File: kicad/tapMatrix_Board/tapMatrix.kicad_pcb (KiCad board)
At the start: 2 copper layers, 68.6 x 53.3 mm, 31 parts, among them P5 TS_ZIF, P6 LED_MATRIX_HDR, U1 MCP1703, U2 MCP4921-E/SN, U3 74LS125, U4 TS922, U5 SD_CARD, U6 DS3231

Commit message: Rough placement of footprints
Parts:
- removed JP7: 6_PIN_3, tapmatrix:Pin_Header_Straight_1x06
- added C10: 47uF, CAP_MVA_F55, F.Cu at (162.8, 128.3)
- added C11: 47uF, CAP_MVA_F55, F.Cu at (184.2, 128.4)
- added C12: 0.1uF, tapmatrix:C_0603, F.Cu at (183.9, 123.4)
- added C13: 0.1uF, tapmatrix:C_0603, F.Cu at (158.9, 109.1)
- added C14: 0.1uF, tapmatrix:C_0603, F.Cu at (143.5, 86.5)
- added C15: 47pF, tapmatrix:C_0603, F.Cu at (143.5, 88.9)
- added C16: 47pF, tapmatrix:C_0603, F.Cu at (143.5, 91.3)
- added C17: 4.7uF, EEE-0JA101WR, F.Cu at (134.6, 99.9)
- added C18: 0.1uF, tapmatrix:C_0603, F.Cu at (143.5, 93.3)
- added C19: 0.1uF, tapmatrix:C_0603, F.Cu at (143.5, 95.4)
- added D1: DIODE, DS16004, F.Cu at (153.7, 126.7)
- added D2: LED, D_0603, F.Cu at (190.6, 129.9)
- added D3: LED, D_0603, F.Cu at (153.0, 105.8)
- added D4: TXLED, D_0603, F.Cu at (146.1, 106.0)
- added D5: RXLED, D_0603, F.Cu at (143.9, 98.9)
- added F1: 500mA, Fuse_MF_MSMF, F.Cu at (156.1, 87.5)
- added P1: +9V Power, tapmatrix:PJ-102AH, F.Cu at (144.7, 132.2)
- added P2: USB-MINI-B, tapmatrix:USBMiniB_UX60_MB_5S8, F.Cu at (138.3, 90.2)
- added R10: 1K, tapmatrix:R_0603, F.Cu at (146.9, 98.9)
- added R11: 10K, tapmatrix:R_0603, F.Cu at (158.5, 102.0)
- added R12: 1K, tapmatrix:R_0603, F.Cu at (161.2, 102.0)
- added R13: 10K, tapmatrix:R_0603, F.Cu at (163.7, 102.0)
- added R14: 1K, tapmatrix:R_0603, F.Cu at (141.2, 98.9)
- added R15: 1K, R_0603, F.Cu at (141.2, 105.9)
- added R6: 510, tapmatrix:R_0603, F.Cu at (190.5, 125.3)
- added R7: 510, tapmatrix:R_0603, F.Cu at (150.2, 105.8)
- added R8: 27, tapmatrix:R_0603, F.Cu at (150.1, 89.2)
- added R9: 27, tapmatrix:R_0603, F.Cu at (150.1, 94.0)
- added SW1: SW_PUSH, SW_3BU_1000P, F.Cu at (162.8, 87.5)
- added U10: 2N7002PW, tapmatrix:SOT-323, F.Cu at (162.7, 97.3)
- added U7: NCP1117ST50T3G, SOT223_318H, F.Cu at (169.7, 128.4)
- added U8: ATMEGA328P-A, tapmatrix:TQFP-32_7x7mm_Pitch0.8mm, F.Cu at (166.1, 114.2)
- added U9: FT231XS, SSOP20_FTDI231X, F.Cu at (156.0, 95.1)
- added X1: CRYSTAL_SMD, XTAL_CSTCE_V, F.Cu at (173.6, 118.7)
- BT1: value CR2032 -> BATTERY
- C4, C6, C9: footprint tapmatrix:EEE-0JA101WR -> EEE-0JA101WR
- JP1: value 6_PIN_1 -> FTDI
- JP2: value 6_PIN_2 -> nRF8001; footprint tapmatrix:Pin_Header_Straight_1x06 -> tapmatrix:Pin_Header_Straight_1x10
- JP3: value 8_PIN_1 -> ICSP; footprint tapmatrix:Pin_Header_Straight_1x08 -> tapmatrix:Pin_Header_Straight_2x03
- JP4: value 8_PIN_2 -> 4_PIN_2
- U2: footprint SOIC-8_N -> tapmatrix:SOIC-8_N
- U3: value 74LS125 -> 74AHC125
- U4: footprint TS922_SO8 -> tapmatrix:TS922_SO8
- U5: footprint 114-00841-68 -> tapmatrix:114-00841-68; moved to B.Cu
- U6: moved to B.Cu
- moved P5 57.0 mm to (189.1, 96.0), turned to 90 degrees
- moved C4 46.0 mm to (134.7, 118.7), turned to 90 degrees
- moved JP6 42.7 mm to (184.9, 104.4), turned to 90 degrees
- moved C6 40.8 mm to (134.7, 109.1), turned to 90 degrees
- moved C9 38.0 mm to (177.4, 96.1)
- moved C2 38.0 mm to (143.3, 120.7)
- moved JP5 37.7 mm to (184.9, 95.6), turned to 270 degrees
- moved C3 34.5 mm to (143.3, 115.7)
- moved RV1 33.5 mm to (191.5, 104.3)
- moved R5 31.4 mm to (158.0, 121.7), turned to 90 degrees
- moved C1 29.6 mm to (143.1, 125.0), turned to 0 degrees
- moved U1 25.9 mm to (136.1, 125.2), turned to 270 degrees
- moved U3 22.4 mm to (152.1, 115.1), turned to 270 degrees
- moved C5 22.1 mm to (143.5, 110.4)
- moved U5 21.6 mm to (132.2, 107.8), turned to 90 degrees
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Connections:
- JP1 pad 1: Net-(JP1-Pad1) -> GND
- JP1 pad 2: Net-(JP1-Pad2) -> GND
- JP1 pad 4: GND -> /MATRIX_CS
- JP1 pad 5: GND -> /MATRIX_CLK
- JP1 pad 6: Net-(JP1-Pad6) -> /RESET
- JP2 pad 1: /XM -> /SCK
- JP2 pad 2: /YP -> /MISO
- JP2 pad 3: /XP -> /MOSI
- JP2 pad 4: /YM -> /D8
- JP2 pad 5: /I2C_SDA -> /DAC_SCK
- JP2 pad 6: /I2C_SCL -> Net-(JP2-Pad6)
- JP3 pad 1: Net-(JP3-Pad1) -> /MISO
- JP3 pad 2: GND -> +5V
- JP3 pad 4: /MISO -> /MOSI
- JP3 pad 5: /MOSI -> /RESET
- JP3 pad 6: /SD_CS -> GND
- JP4 pad 1: /MATRIX_DATA -> /I2C_SDA
- JP4 pad 2: /MATRIX_WR -> /I2C_SCL
- JP4 pad 3: /DAC_LAT -> +3.3V
- JP4 pad 4: /DAC_DI -> GND
- JP4 pad 5: /DAC_SCK -> (no net)
- JP4 pad 6: /DAC_CS -> (no net)
- JP4 pad 7: /MATRIX_CS -> (no net)
- JP4 pad 8: /MATRIX_CLK -> (no net)
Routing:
- net +3.3V: track 112.0 -> 0.00 mm, vias 2 -> 0
- net /I2C_SDA: track 96.3 -> 0.00 mm, vias 3 -> 0
- net /I2C_SCL: track 79.2 -> 0.00 mm, vias 6 -> 0
- net GND: track 76.8 -> 0.00 mm, vias 18 -> 0
- net /YM: track 56.1 -> 0.00 mm, vias 2 -> 0
- net Net-(BT1-Pad1): track 53.6 -> 0.00 mm, vias 2 -> 0
- net Net-(C9-Pad1): track 51.3 -> 0.00 mm, vias 4 -> 0
- net /XP: track 51.0 -> 0.00 mm, vias 2 -> 0
- net /YP: track 46.0 -> 0.00 mm, vias 2 -> 0
- net /XM: track 40.3 -> 0.00 mm, vias 2 -> 0
- net /SCLK: track 35.6 -> 0.00 mm, vias 2 -> 0
- net /DATA_IN: track 31.8 -> 0.00 mm, vias 2 -> 0
- net /CS: track 31.0 -> 0.00 mm
- net /MISO: track 30.6 -> 0.00 mm, vias 1 -> 0
- net /MATRIX_DATA: track 29.4 -> 0.00 mm
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- removed copper zone on F.Cu, net +5V
- removed copper zone on B.Cu, net GND
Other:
- board text removed: "(c) 2015 Responsive Devices Inc"
- board text removed: "3V3"
- board text removed: "5V0"
- board text removed: "922IY ST"
- board text removed: "SPK+"
- board text removed: "SPK-"
- board text removed: "XM"
- board text removed: "XP"
- board text removed: "YM"
- board text removed: "YP"
- board text removed: "tapMatrix Shield 0.4.1 Feb 2015"

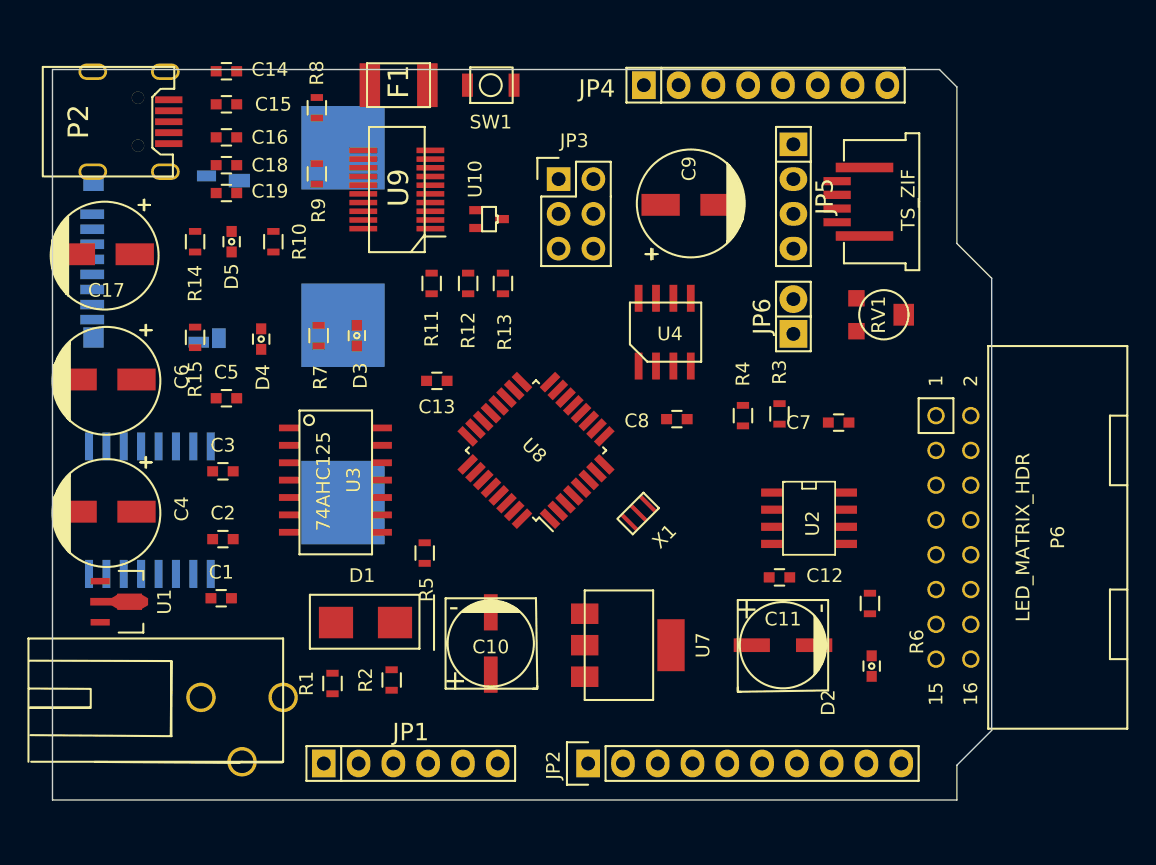
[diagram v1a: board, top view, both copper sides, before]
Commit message: add C20, begin routing
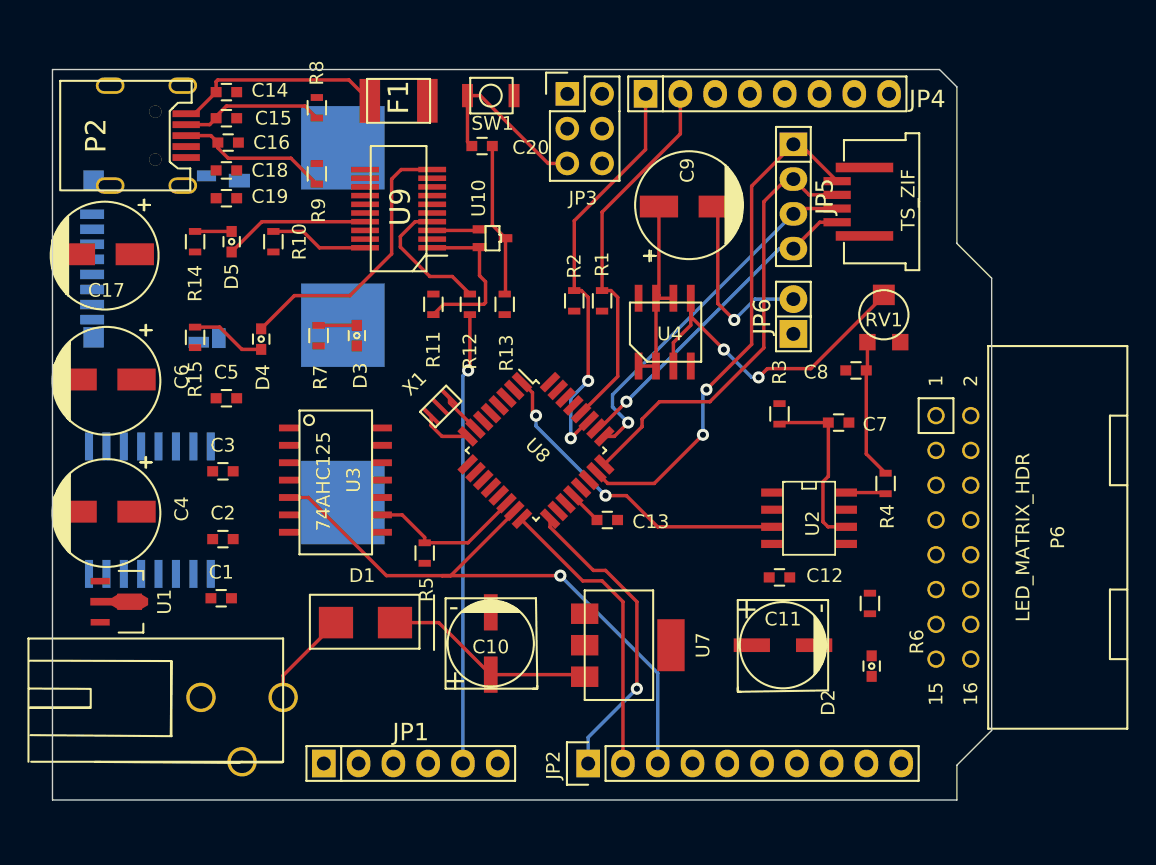
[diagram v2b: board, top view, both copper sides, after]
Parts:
- added C20: 0.1uF, tapmatrix:C_0603, F.Cu at (162.2, 91.9)
- moved R1 34.2 mm to (170.9, 103.3)
- moved R2 30.7 mm to (168.9, 103.3)
- moved X1 16.4 mm to (159.1, 111.0), turned to 225 degrees
- moved C13 16.1 mm to (171.3, 119.3), turned to 0 degrees
- moved C8 13.6 mm to (189.5, 108.3)
- moved R4 11.5 mm to (191.6, 116.6)
- moved JP3 6.26 mm to (168.4, 88.1)
- moved P2 1.63 mm to (139.6, 91.2)
- moved R13 1.53 mm to (163.8, 103.5)
- moved R11 1.53 mm to (158.6, 103.5)
- moved R12 1.53 mm to (161.3, 103.5)
- moved C14 1.52 mm to (143.5, 88.0)
- moved U10 1.42 mm to (162.9, 98.7)
- moved U9 1.40 mm to (156.1, 96.5)
- moved F1 1.14 mm to (156.1, 88.6)
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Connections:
- net +3.3V renamed VCC
- R13 pad 2: /RESET -> Net-(C20-Pad2)
- U10 pad 3: /RESET -> Net-(C20-Pad2)
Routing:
- net /MOSI: track 0.00 -> 46.1 mm, vias 0 -> 1
- net /XM: track 0.00 -> 37.8 mm, vias 0 -> 2
- net /MATRIX_CLK: track 0.00 -> 33.0 mm, vias 0 -> 1
- net /YP: track 0.00 -> 32.7 mm
- net /I2C_SDA: track 0.00 -> 30.4 mm, vias 0 -> 2
- net /I2C_SCL: track 0.00 -> 27.6 mm
- net /XP: track 0.00 -> 26.7 mm, vias 0 -> 1
- net Net-(RV1-Pad2): track 0.00 -> 25.3 mm, vias 0 -> 2
- net /DAC_SCK: track 0.00 -> 23.9 mm, vias 0 -> 2
- net /YM: track 0.00 -> 23.8 mm, vias 0 -> 1
- net /SCK: track 0.00 -> 22.5 mm, vias 0 -> 1
- net /MISO: track 0.00 -> 21.8 mm
- net Net-(D4-Pad2): track 0.00 -> 20.5 mm
- net Net-(C14-Pad1): track 0.00 -> 15.5 mm
- net Net-(C10-Pad1): track 0.00 -> 15.5 mm
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
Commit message: continue routing top layer
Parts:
- moved D1 3.70 mm to (152.3, 130.2), turned to 90 degrees
- moved C10 2.33 mm to (161.9, 130.4)
- moved D2 0.13 mm to (190.5, 129.9), turned to 270 degrees
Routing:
- net /MATRIX_CS: track 0.00 -> 103.6 mm, vias 0 -> 4
- net /MISO: track 21.8 -> 111.7 mm, vias 0 -> 3
- net /SCK: track 22.5 -> 110.0 mm, vias 1 -> 9
- net /MOSI: track 46.1 -> 127.7 mm, vias 1 -> 3
- net /RESET: track 13.2 -> 84.5 mm, vias 0 -> 4
- net /DAC_CS: track 0.00 -> 58.3 mm, vias 0 -> 2
- net /MATRIX_CLK: track 33.0 -> 80.3 mm, vias 1 -> 4
- net /D9: track 0.00 -> 43.6 mm, vias 0 -> 1
- net /MATRIX_WR: track 0.00 -> 43.1 mm, vias 0 -> 1
- net /D8: track 0.00 -> 42.0 mm, vias 0 -> 2
- net /MATRIX_DATA: track 0.00 -> 38.8 mm, vias 0 -> 1
- net /DAC_LAT: track 0.00 -> 32.2 mm, vias 0 -> 4
- net /DAC_DI: track 0.00 -> 27.1 mm, vias 0 -> 2
- net /DAC_SCK: track 23.9 -> 45.6 mm
- net /I2C_SDA: track 30.4 -> 37.0 mm, vias 2 -> 4
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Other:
- board text added: "this should be 4, not 8"

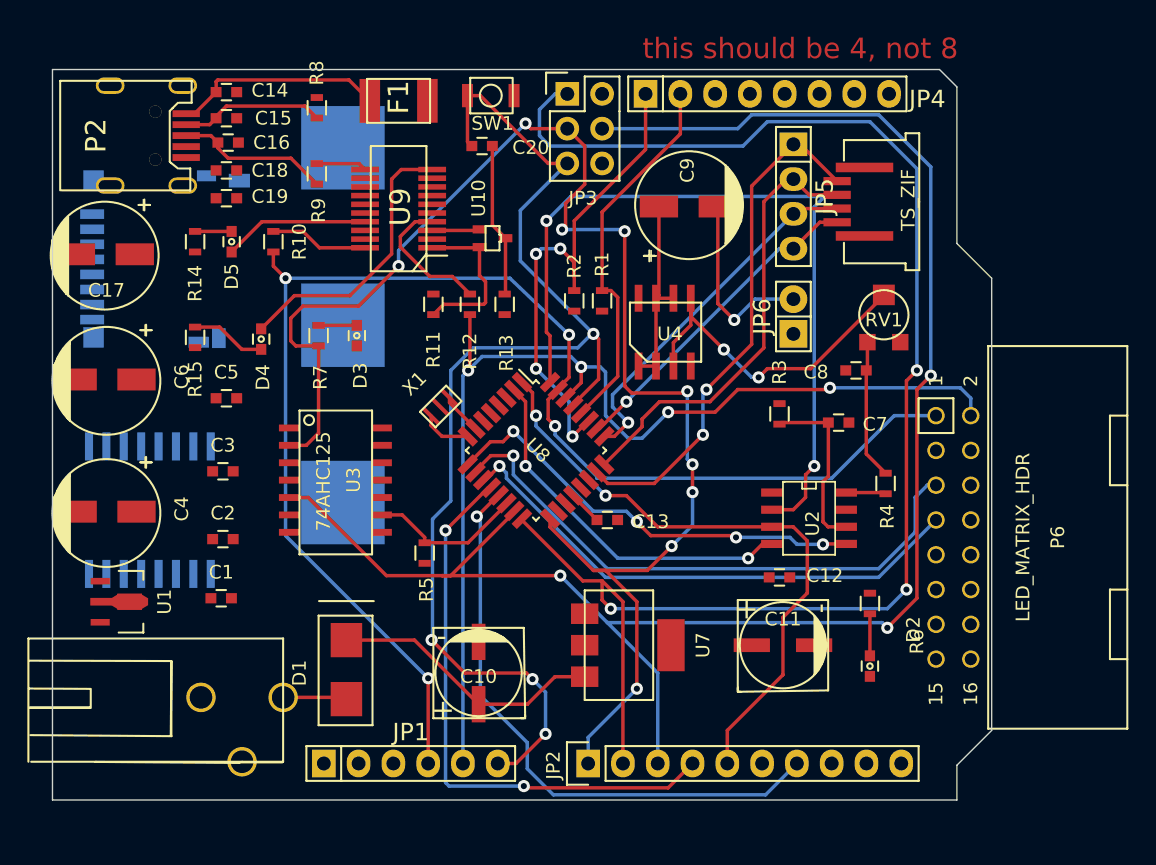
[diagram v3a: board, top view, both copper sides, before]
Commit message: Complete first pass routing
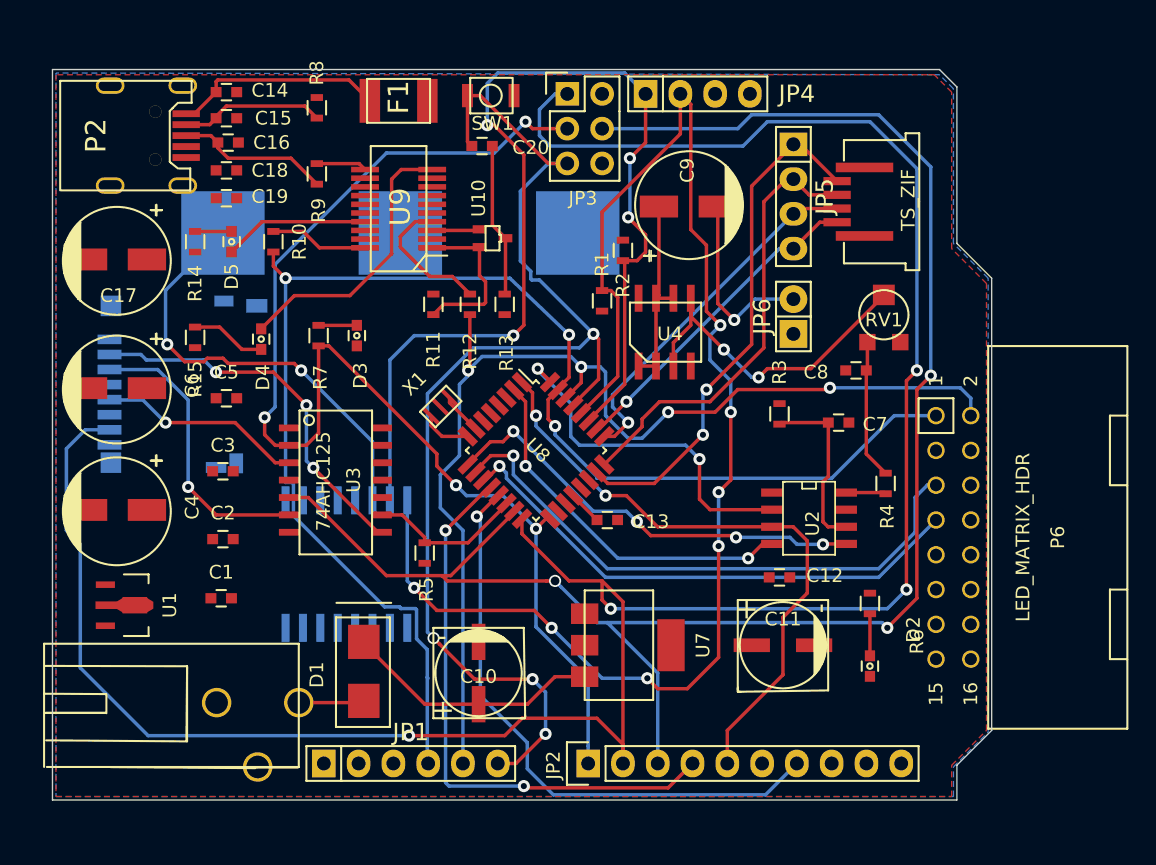
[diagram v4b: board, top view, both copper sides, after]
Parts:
- JP4: footprint tapmatrix:Pin_Header_Straight_1x08 -> tapmatrix:Pin_Header_Straight_1x04
- moved U6 14.9 mm to (152.5, 122.2)
- moved U5 9.23 mm to (133.5, 117.0)
- moved BT1 7.93 mm to (156.2, 98.3), turned to 180 degrees
- moved R2 5.12 mm to (172.5, 99.6), turned to 270 degrees
- moved JP4 5.08 mm to (177.9, 88.1)
- moved D1 1.28 mm to (153.5, 130.3)
- moved P1 1.20 mm to (145.8, 132.6)
- moved C6 0.99 mm to (135.5, 109.7)
- moved C17 0.97 mm to (135.5, 100.3)
- moved C4 0.77 mm to (135.5, 118.6)
- moved U1 0.46 mm to (136.5, 125.5)
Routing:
- net /I2C_SCL: track 27.6 -> 104.1 mm, vias 0 -> 7
- net /MISO: track 111.7 -> 176.8 mm, vias 3 -> 4
- net /I2C_SDA: track 37.0 -> 80.1 mm
- net /DAC_CS: track 58.3 -> 25.9 mm
- net Net-(BT1-Pad1): track 0.00 -> 32.3 mm, vias 0 -> 2
- net /CS: track 0.00 -> 27.6 mm, vias 0 -> 3
- net /DATA_IN: track 0.00 -> 21.2 mm, vias 0 -> 1
- net /SCK: track 110.0 -> 91.6 mm, vias 9 -> 4
- net /SCLK: track 0.00 -> 15.0 mm, vias 0 -> 1
- net /MATRIX_CS: track 103.6 -> 105.3 mm, vias 4 -> 3
- net /MATRIX_CLK: track 80.3 -> 81.7 mm
- net Net-(C10-Pad1): track 20.4 -> 19.1 mm
- net /RESET: track 84.5 -> 85.7 mm
- added copper zone on F.Cu, net +5V
- added copper zone on B.Cu, net GND
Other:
- board text removed: "this should be 4, not 8"

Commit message: Complete routing of 4-layer board
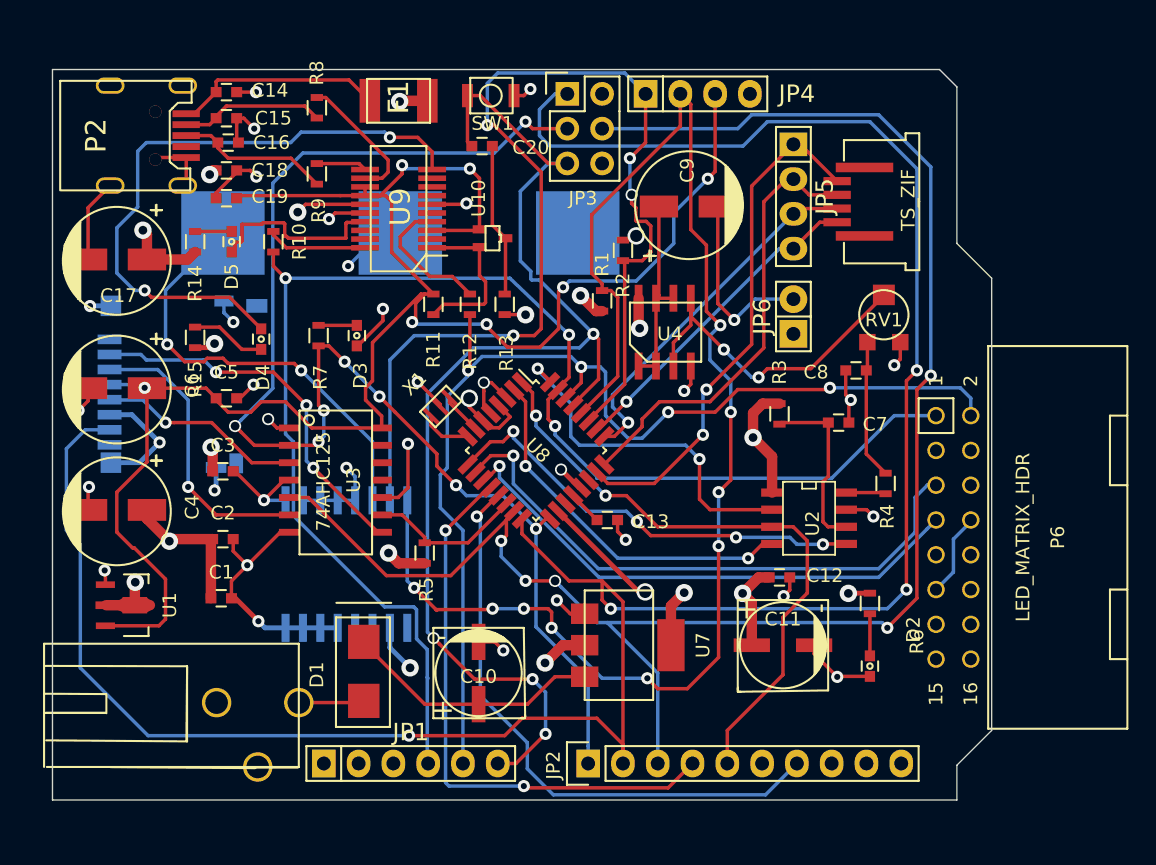
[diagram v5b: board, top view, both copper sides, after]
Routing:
- net VCC: track 3.49 -> 135.6 mm, vias 0 -> 7
- net GND: track 0.00 -> 132.0 mm, vias 0 -> 34
- net +5V: track 0.00 -> 86.1 mm, vias 0 -> 21
- net Net-(D4-Pad2): track 20.5 -> 45.7 mm, vias 0 -> 2
- net Net-(R8-Pad2): track 0.00 -> 9.86 mm
- net /SCK: track 91.6 -> 98.5 mm, vias 4 -> 8
- net Net-(D5-Pad2): track 10.7 -> 13.8 mm
- net /I2C_SDA: track 80.1 -> 83.3 mm
- net /I2C_SCL: track 104.1 -> 105.6 mm, vias 7 -> 9
- net /MOSI: track 127.7 -> 126.8 mm, vias 3 -> 5
- added copper zone on In1.Cu, net +5V
- added copper zone on In2.Cu, net GND
- removed copper zone on F.Cu, net +5V
- removed copper zone on B.Cu, net GND
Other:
- copper layers 2 -> 4
- net class Power: clearance 0.381 -> 0.3
